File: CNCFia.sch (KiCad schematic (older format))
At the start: 19 parts, among them J1 GND, J10 Driver_X, J11 Driver_Y, J12 Driver_Z, J14 Spin_10V, J15 Relay_1, J16 Relay_2, J17 Relay_3, J2 EXT_5V, J3 Limit SW_XY, J4 Limit SW_ZA, J5 Extra SW 0, J6 Extra SW 1, J7 EXT_12V, J8 OPTO_5V, J9 Signal Input

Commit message: Renamed Kicad Project, cleanup
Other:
- moved on the sheet: J14, J15, J16, J17

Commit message: Pre-SMD
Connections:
- net +5V: now also J1.2
- net GND: no longer J1.2
- net LV_1 renamed X_Enbl
- net LV_2 renamed X_Dir
- net LV_3 renamed X_Step
- net LV_4 renamed Y_Enbl
- net LV_5 renamed Y_Dir
- net LV_6 renamed Y_Step
- net LV_7 renamed Z_Enbl
- net LV_8 renamed Z_Dir
- net LV_9 renamed Z_Step
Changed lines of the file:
@@
 Title "CNC Generic Daughter Card"
 Date "2020-01-26"
-Rev "1"
+Rev "10"
 Comp "c6p"
 Comment1 ""
@@
 F 3 "" H 1500 5500 50  0001 C CNN
 	1    1500 5500
-	1    0    0    -1
-$EndComp
-$Comp
-L power:GND #PWR02
-U 1 1 5E3933B0
-P 1800 5500
-F 0 "#PWR02" H 1800 5250 50  0001 C CNN
-F 1 "GND" H 1805 5327 50  0000 C CNN
-F 2 "" H 1800 5500 50  0001 C CNN
-F 3 "" H 1800 5500 50  0001 C CNN
-	1    1800 5500
 	1    0    0    -1
 $EndComp
@@
 Text GLabel 6150 1950 1    50   Input ~ 0
 MCU_5V
-Wire Wire Line
-	2400 5500 2400 5650
 $Comp
 L power:PWR_FLAG #FLG06
@@
 Wire Wire Line
 	1950 7000 1950 7100
-$Comp
-L power:PWR_FLAG #FLG02
-U 1 1 5E46D8BB
-P 2650 5650
-F 0 "#FLG02" H 2650 5725 50  0001 C CNN
-F 1 "PWR_FLAG" H 2650 5823 50  0000 C CNN
-F 2 "" H 2650 5650 50  0001 C CNN
-F 3 "~" H 2650 5650 50  0001 C CNN
-	1    2650 5650
-	1    0    0    -1
-$EndComp
-Wire Wire Line
-	2650 5650 2400 5650
-Connection ~ 2400 5650
-Wire Wire Line
-	2400 5650 2400 5700
-Wire Wire Line
-	1700 5500 1800 5500
 Wire Wire Line
 	1600 5500 1500 5500
@@
 $EndComp
 $Comp
-L power:PWR_FLAG #FLG03
-U 1 1 5E4CD356
-P 3800 5750
-F 0 "#FLG03" H 3800 5825 50  0001 C CNN
-F 1 "PWR_FLAG" H 3800 5923 50  0000 C CNN
-F 2 "" H 3800 5750 50  0001 C CNN
-F 3 "~" H 3800 5750 50  0001 C CNN
-	1    3800 5750
-	1    0    0    -1
-$EndComp
-Wire Wire Line
-	3800 5750 3450 5750
-Connection ~ 3450 5750
-$Comp
 L power:PWR_FLAG #FLG07
 U 1 1 5E4D45DE
@@
 	9450 1950 9150 1950
 Connection ~ 9150 1950
-$Comp
-L SamacSys_Parts:TB008A-508-02BE J1
-U 1 1 5E532367
-P 1600 5500
-F 0 "J1" H 2228 5496 50  0000 L CNN
-F 1 "GND" H 2228 5405 50  0000 L CNN
-F 2 "Kicad_extra_components:CUI_TBP01R2-508-02BE" H 2250 5600 50  0001 L CNN
-F 3 "https://componentsearchengine.com/Datasheets/1/TB008A-508-02BE.pdf" H 2250 5500 50  0001 L CNN
-F 4 "Fixed Terminal Blocks screw type, 5.08 , 45 , 2 poles, CUI Blue, slotted screw, PCB mount" H 2250 5400 50  0001 L CNN "Description"
-F 5 "15.82" H 2250 5300 50  0001 L CNN "Height"
-F 6 "490-TB008A-508-02BE" H 2250 5200 50  0001 L CNN "Mouser Part Number"
-F 7 "https://www.mouser.com/Search/Refine.aspx?Keyword=490-TB008A-508-02BE" H 2250 5100 50  0001 L CNN "Mouser Price/Stock"
-F 8 "CUI" H 2250 5000 50  0001 L CNN "Manufacturer_Name"
-F 9 "TB008A-508-02BE" H 2250 4900 50  0001 L CNN "Manufacturer_Part_Number"
-F 10 "102-6422-ND" H 1600 5500 50  0001 C CNN "Digi-Key_PN"
-F 11 "  	TBP01R2-508-02BE " H 1600 5500 50  0001 C CNN "MPN"
-F 12 "TBP01R2-508-02BE " H 1600 5500 50  0001 C CNN "Manufacturer"
-F 13 "production" H 1600 5500 50  0001 C CNN "fit_field"
-F 14 "production" H 1600 5500 50  0001 C CNN "Config"
-	1    1600 5500
-	0    -1   -1   0
-$EndComp
 $Comp
 L SamacSys_Parts:TB008A-508-02BE J2
@@
 	1    0    0    -1
 $EndComp
-$Comp
-L power:PWR_FLAG #FLG01
-U 1 1 5E3C8F16
-P 2100 5650
-F 0 "#FLG01" H 2100 5725 50  0001 C CNN
-F 1 "PWR_FLAG" H 2100 5823 50  0000 C CNN
-F 2 "" H 2100 5650 50  0001 C CNN
-F 3 "~" H 2100 5650 50  0001 C CNN
-	1    2100 5650
-	1    0    0    -1
-$EndComp
-Wire Wire Line
-	2100 5650 2250 5650
-Connection ~ 2250 5650
 Text GLabel 4500 5700 3    50   Input ~ 0
 OPTO_5V
@@
 Wire Wire Line
 	4400 5550 4350 5550
-Wire Wire Line
-	4350 5550 4350 5650
-Wire Wire Line
-	4500 5500 4500 5650
-$Comp
-L power:PWR_FLAG #FLG05
-U 1 1 5E87F031
-P 4750 5650
-F 0 "#FLG05" H 4750 5725 50  0001 C CNN
-F 1 "PWR_FLAG" H 4750 5823 50  0000 C CNN
-F 2 "" H 4750 5650 50  0001 C CNN
-F 3 "~" H 4750 5650 50  0001 C CNN
-	1    4750 5650
-	1    0    0    -1
-$EndComp
-Wire Wire Line
-	4750 5650 4500 5650
-Connection ~ 4500 5650
-Wire Wire Line
-	4500 5650 4500 5700
 $Comp
 L SamacSys_Parts:TB008A-508-02BE J8
@@
 	0    -1   -1   0
 $EndComp
-$Comp
-L power:PWR_FLAG #FLG04
-U 1 1 5E87F04F
-P 4200 5650
-F 0 "#FLG04" H 4200 5725 50  0001 C CNN
-F 1 "PWR_FLAG" H 4200 5823 50  0000 C CNN
-F 2 "" H 4200 5650 50  0001 C CNN
-F 3 "~" H 4200 5650 50  0001 C CNN
-	1    4200 5650
-	1    0    0    -1
-$EndComp
-Wire Wire Line
-	4200 5650 4350 5650
 Text GLabel 4350 5700 3    50   Input ~ 0
 OPTO_GND
-Wire Wire Line
-	4350 5700 4350 5650
-Connection ~ 4350 5650
 Text GLabel 5300 7200 1    50   Input ~ 0
 EXT_5V
@@
 Extra_SW
 Text GLabel 7550 2150 0    50   Input ~ 0
-LV_1
+X_Enbl
 Text GLabel 7550 2250 0    50   Input ~ 0
-LV_2
+X_Dir
 Text GLabel 7550 2350 0    50   Input ~ 0
-LV_3
-Text GLabel 7550 2450 0    50   Input ~ 0
-LV_4
-Text GLabel 7550 2550 0    50   Input ~ 0
-LV_5
-Text GLabel 7550 2650 0    50   Input ~ 0
-LV_6
-Text GLabel 7550 2750 0    50   Input ~ 0
-LV_7
-Text GLabel 7550 2850 0    50   Input ~ 0
-LV_8
-Text GLabel 7550 2950 0    50   Input ~ 0
-LV_9
-Text GLabel 5900 2150 2    50   Input ~ 0
-LV_1
-Text GLabel 5900 2250 2    50   Input ~ 0
-LV_2
-Text GLabel 5900 2350 2    50   Input ~ 0
-LV_3
-Text GLabel 5900 2450 2    50   Input ~ 0
-LV_4
-Text GLabel 5900 2550 2    50   Input ~ 0
-LV_5
-Text GLabel 5900 2650 2    50   Input ~ 0
-LV_6
-Text GLabel 5900 2750 2    50   Input ~ 0
-LV_7
-Text GLabel 5900 2850 2    50   Input ~ 0
-LV_8
-Text GLabel 5900 2950 2    50   Input ~ 0
-LV_9
+X_Step
 Text GLabel 7300 3850 0    50   Input ~ 0
 SPIN_PWM
@@
 	1    0    0    -1
 $EndComp
+Text GLabel 7550 2450 0    50   Input ~ 0
+Y_Enbl
+Text GLabel 7550 2550 0    50   Input ~ 0
+Y_Dir
+Text GLabel 7550 2650 0    50   Input ~ 0
+Y_Step
+Text GLabel 7550 2750 0    50   Input ~ 0
+Z_Enbl
+Text GLabel 7550 2850 0    50   Input ~ 0
+Z_Dir
+Text GLabel 7550 2950 0    50   Input ~ 0
+Z_Step
+Text GLabel 5900 2150 2    50   Input ~ 0
+X_Enbl
+Text GLabel 5900 2250 2    50   Input ~ 0
+X_Dir
+Text GLabel 5900 2350 2    50   Input ~ 0
+X_Step
+Text GLabel 5900 2450 2    50   Input ~ 0
+Y_Enbl
+Text GLabel 5900 2550 2    50   Input ~ 0
+Y_Dir
+Text GLabel 5900 2650 2    50   Input ~ 0
+Y_Step
+Text GLabel 5900 2750 2    50   Input ~ 0
+Z_Enbl
+Text GLabel 5900 2850 2    50   Input ~ 0
+Z_Dir
+Text GLabel 5900 2950 2    50   Input ~ 0
+Z_Step
+$Comp
+L SamacSys_Parts:TB008A-508-02BE J1
+U 1 1 5E532367
+P 1600 5500
+F 0 "J1" H 2228 5496 50  0000 L CNN
+F 1 "GND" H 2228 5405 50  0000 L CNN
+F 2 "Kicad_extra_components:CUI_TBP01R2-508-02BE" H 2250 5600 50  0001 L CNN
+F 3 "https://componentsearchengine.com/Datasheets/1/TB008A-508-02BE.pdf" H 2250 5500 50  0001 L CNN
+F 4 "Fixed Terminal Blocks screw type, 5.08 , 45 , 2 poles, CUI Blue, slotted screw, PCB mount" H 2250 5400 50  0001 L CNN "Description"
+F 5 "15.82" H 2250 5300 50  0001 L CNN "Height"
+F 6 "490-TB008A-508-02BE" H 2250 5200 50  0001 L CNN "Mouser Part Number"
+F 7 "https://www.mouser.com/Search/Refine.aspx?Keyword=490-TB008A-508-02BE" H 2250 5100 50  0001 L CNN "Mouser Price/Stock"
+F 8 "CUI" H 2250 5000 50  0001 L CNN "Manufacturer_Name"
+F 9 "TB008A-508-02BE" H 2250 4900 50  0001 L CNN "Manufacturer_Part_Number"
+F 10 "102-6422-ND" H 1600 5500 50  0001 C CNN "Digi-Key_PN"
+F 11 "  	TBP01R2-508-02BE " H 1600 5500 50  0001 C CNN "MPN"
+F 12 "TBP01R2-508-02BE " H 1600 5500 50  0001 C CNN "Manufacturer"
+F 13 "production" H 1600 5500 50  0001 C CNN "fit_field"
+F 14 "production" H 1600 5500 50  0001 C CNN "Config"
+	1    1600 5500
+	0    -1   -1   0
+$EndComp
+$Comp
+L power:+5V #PWR?
+U 1 1 5E3F3104
+P 1800 5650
+AR Path="/5E2EF045/5E3F3104" Ref="#PWR?"  Part="1"
+AR Path="/5E3F3104" Ref="#PWR0102"  Part="1"
+F 0 "#PWR0102" H 1800 5500 50  0001 C CNN
+F 1 "+5V" H 1815 5823 50  0000 C CNN
+F 2 "" H 1800 5650 50  0001 C CNN
+F 3 "" H 1800 5650 50  0001 C CNN
+	1    1800 5650
+	1    0    0    -1
+$EndComp
+Wire Wire Line
+	1700 5650 1700 5500
+Wire Wire Line
+	1800 5650 1700 5650
+Wire Wire Line
+	2400 5500 2400 5700
+Wire Wire Line
+	4350 5550 4350 5700
+Wire Wire Line
+	4500 5500 4500 5700
 $EndSCHEMATC

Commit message: Makes it SMD based, with smaller connectors
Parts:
- added J13: Coolant, Kicad_extra_components:CUI_TBP02R2-381-03BE, symbol SamacSys_Parts:TB008A-508-03BE
- added R5, R6: 2k2, Resistor_SMD:R_1206_3216Metric_Pad1.42x1.75mm_HandSolder, symbol Device:R_US
- added U6: 24LC16, Package_SO:SOIC-8_3.9x4.9mm_P1.27mm, symbol Memory_EEPROM:24LC16
- J1, J14, J2, J7, J8: footprint Kicad_extra_components:CUI_TBP01R2-508-02BE -> Kicad_extra_components:CUI_TBP02R2-381-02BE
- J10, J11, J12, J6: footprint Kicad_extra_components:CUI_TBP01R2-508-03BE -> Kicad_extra_components:CUI_TBP02R2-381-03BE
- J15: value Relay_1 -> Spin_Enabl; footprint Kicad_extra_components:CUI_TBP01R2-508-03BE -> Kicad_extra_components:CUI_TBP02R2-381-03BE
- J16: value Relay_2 -> Spin_Dir; footprint Kicad_extra_components:CUI_TBP01R2-508-03BE -> Kicad_extra_components:CUI_TBP02R2-381-03BE
- J17: value Relay_3 -> Mist; footprint Kicad_extra_components:CUI_TBP01R2-508-03BE -> Kicad_extra_components:CUI_TBP02R2-381-03BE
- J3, J4, J5: footprint Kicad_extra_components:CUI_TBP01R2-508-04BE -> Kicad_extra_components:CUI_TBP02R2-381-04BE
- J9: footprint Connector_PinHeader_2.54mm:PinHeader_2x15_P2.54mm_Vertical -> Connector_PinHeader_2.54mm:PinHeader_2x20_P2.54mm_Vertical; symbol Connector_Generic:Conn_02x15_Odd_Even -> Connector_Generic:Conn_02x20_Odd_Even; Digi-Key_PN ED10527-ND -> ED10529-ND; MPN (none) -> 302-S401
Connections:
- net +3V3: now also R5.1, R6.1, U6.8 (VCC)
- net Door: now also J5.4; no longer J5.1
- net Feed_Hold: now also J5.2; no longer J5.3
- net GND: now also J5.1, U6.4 (GND), U6.7 (WP); no longer J5.4, J9.29 (Pin_29)
- net Level Shifters/HV_1: now also J10.3; no longer J10.1
- net Level Shifters/HV_3: now also J10.1; no longer J10.3
- net Level Shifters/HV_4: now also J11.3; no longer J11.1
- net Level Shifters/HV_6: now also J11.1; no longer J11.3
- net Level Shifters/HV_7: now also J12.3; no longer J12.1
- net Level Shifters/HV_9: now also J12.1; no longer J12.3
- net Opto-isolated switches/SW_Extra: now also J4.1; no longer J4.4
- net Opto-isolated switches/SW_Probe: now also J4.2; no longer J4.3
- net Opto-isolated switches/SW_XMAX: now also J3.3; no longer J3.2
- net Opto-isolated switches/SW_XMIN: now also J3.4; no longer J3.1
- net Opto-isolated switches/SW_YMAX: now also J3.1; no longer J3.4
- net Opto-isolated switches/SW_YMIN: now also J3.2; no longer J3.3
- net Opto-isolated switches/SW_ZMAX: now also J4.3; no longer J4.2
- net Opto-isolated switches/SW_ZMIN: now also J4.4; no longer J4.1
- net Reset: now also J5.3; no longer J5.2
- net IN_Relay_1 renamed Spin_Enbl
- net IN_Relay_2 renamed Spin_Dir
- net IN_Relay_3 renamed Mist
- net SPIN_PWM renamed Spin_PWM
- new net E_SCL: J9.31 (Pin_31), R5.2, U6.6 (SCL)
- new net E_SDA: J9.29 (Pin_29), R6.2, U6.5 (SDA)
- new net Flood: J9.32 (Pin_32)
- new net Relays/Relay_COM_4: J13.1
- new net Relays/Relay_NC_4: J13.3
- new net Relays/Relay_NO_4: J13.2
- no-connect marks 0 -> 3
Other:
- moved on the sheet: J1, J14, J15, J16, J17, J2, J3, J4, J5, J6, J7, J8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

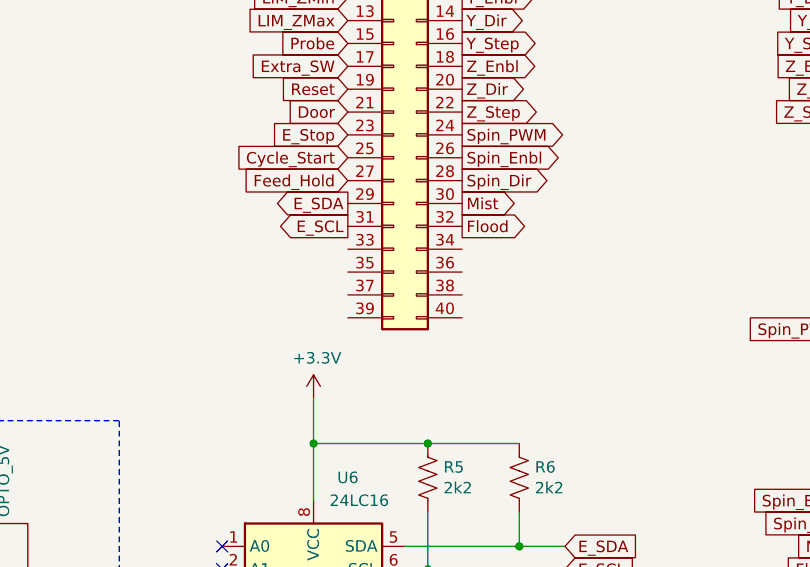
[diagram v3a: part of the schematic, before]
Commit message: Vertical mounted version
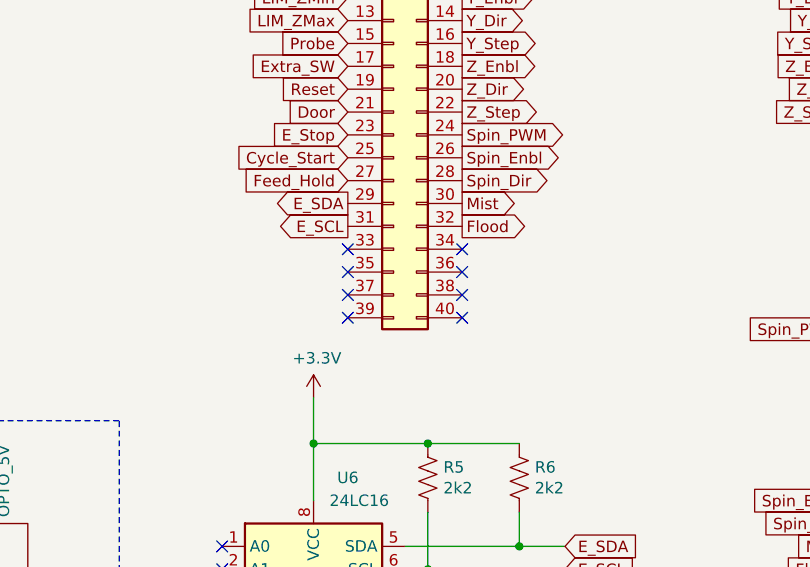
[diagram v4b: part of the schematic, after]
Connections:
- no-connect marks 3 -> 11
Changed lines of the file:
@@
 NoConn ~ 4850 4950
 NoConn ~ 4850 5050
+NoConn ~ 5400 3550
+NoConn ~ 5400 3650
+NoConn ~ 5400 3750
+NoConn ~ 5400 3850
+NoConn ~ 5900 3850
+NoConn ~ 5900 3750
+NoConn ~ 5900 3650
+NoConn ~ 5900 3550
 Wire Wire Line
 	900  7100 900  7050
